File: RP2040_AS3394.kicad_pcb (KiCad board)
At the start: 4 copper layers, 123 parts, among them J1 Conn_01x03, J2 TYPE-C-31-M-12, U1 RP2040, U2 NCP1117-3.3_SOT223, U3 W25Q128JVS, U4 LM324, U5 AS3394, U6 LM324, Y1 X322512MSB4SI

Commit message: Started placement
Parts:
- R3, R4: footprint Resistor_SMD:R_0603_1608Metric -> Resistor_SMD:R_0402_1005Metric
- moved U6 160.7 mm to (181.6, 142.4)
- moved C25 148.5 mm to (172.8, 141.9)
- moved R26 137.7 mm to (169.8, 139.8)
- moved C22 136.3 mm to (165.1, 139.7)
- moved R23 135.9 mm to (165.5, 142.5)
- moved R13 133.7 mm to (158.1, 140.0)
- moved C48 131.6 mm to (178.4, 131.3)
- moved R18 131.1 mm to (161.3, 143.1)
- moved C47 130.0 mm to (178.2, 127.1)
- moved U5 129.0 mm to (131.1, 123.8)
- moved R10 127.3 mm to (155.1, 140.0)
- moved C20 126.0 mm to (162.4, 140.0)
- moved C24 111.1 mm to (83.7, 156.5)
- moved C21 109.4 mm to (75.7, 154.6)
- moved U4 107.5 mm to (102.5, 135.4)
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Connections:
- C22 pad 2: Net-(C22-Pad2) -> Net-(R26-Pad1)
- R23 pad 2: Net-(C22-Pad2) -> Net-(R26-Pad1)
- R26 pad 1: Net-(C22-Pad2) -> Net-(R26-Pad1)
- U4 pad 12: Net-(C20-Pad1) -> GND
- U4 pad 13: Net-(R18-Pad2) -> Net-(R43-Pad2)
- U4 pad 14: Net-(C22-Pad2) -> /AS3394_PWM/Wave_Select_CV
- U6 pad 1: /AS3394_PWM/Wave_Select_CV -> Net-(R26-Pad1)
- U6 pad 2: Net-(R43-Pad2) -> Net-(R18-Pad2)
- U6 pad 3: GND -> Net-(C20-Pad1)

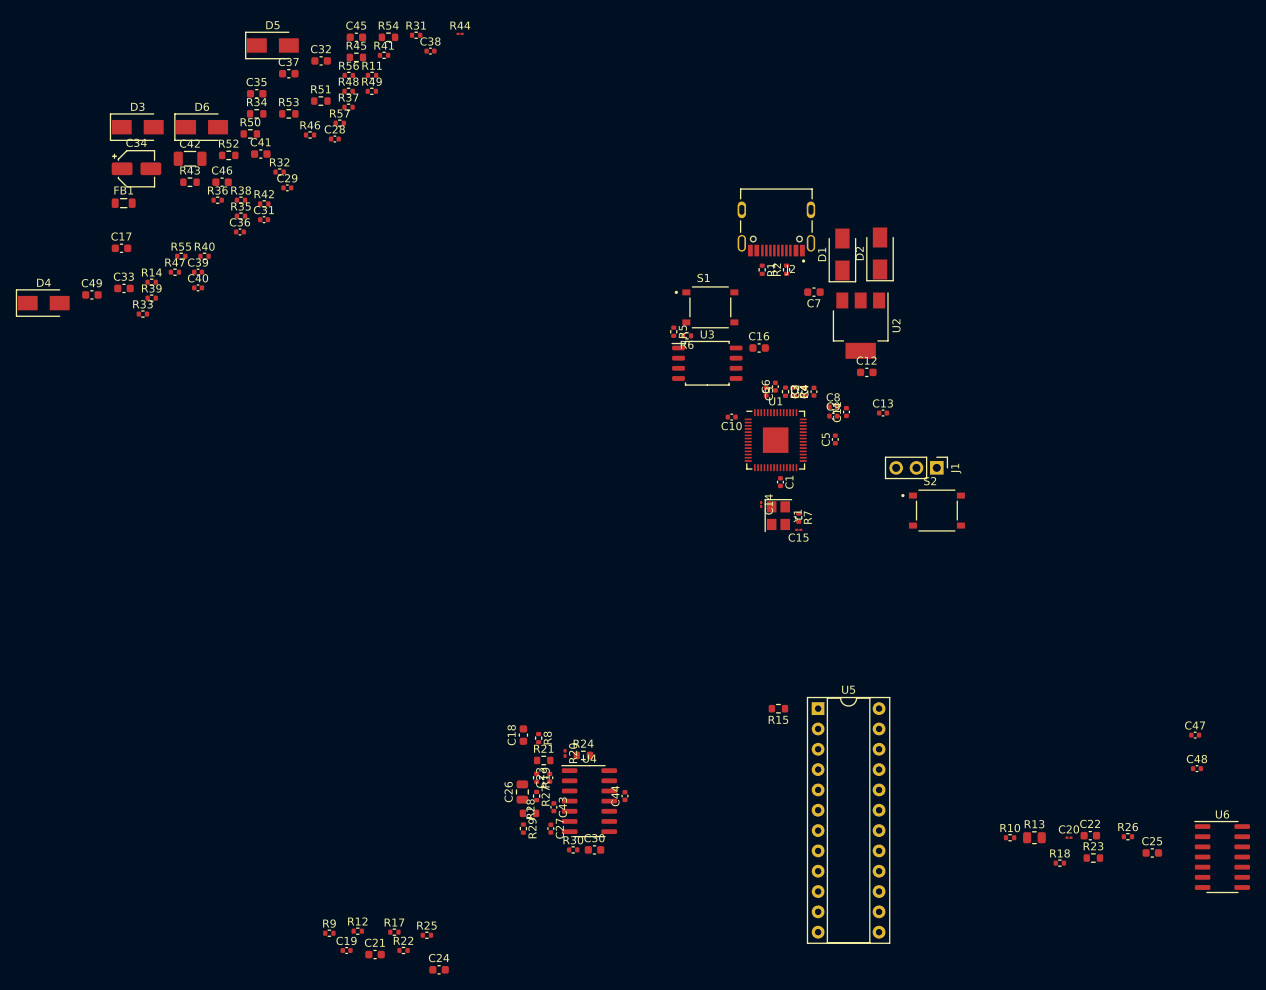
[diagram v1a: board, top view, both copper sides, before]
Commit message: Finished most of routing; added TL071 for headphone out; working on adding I/O
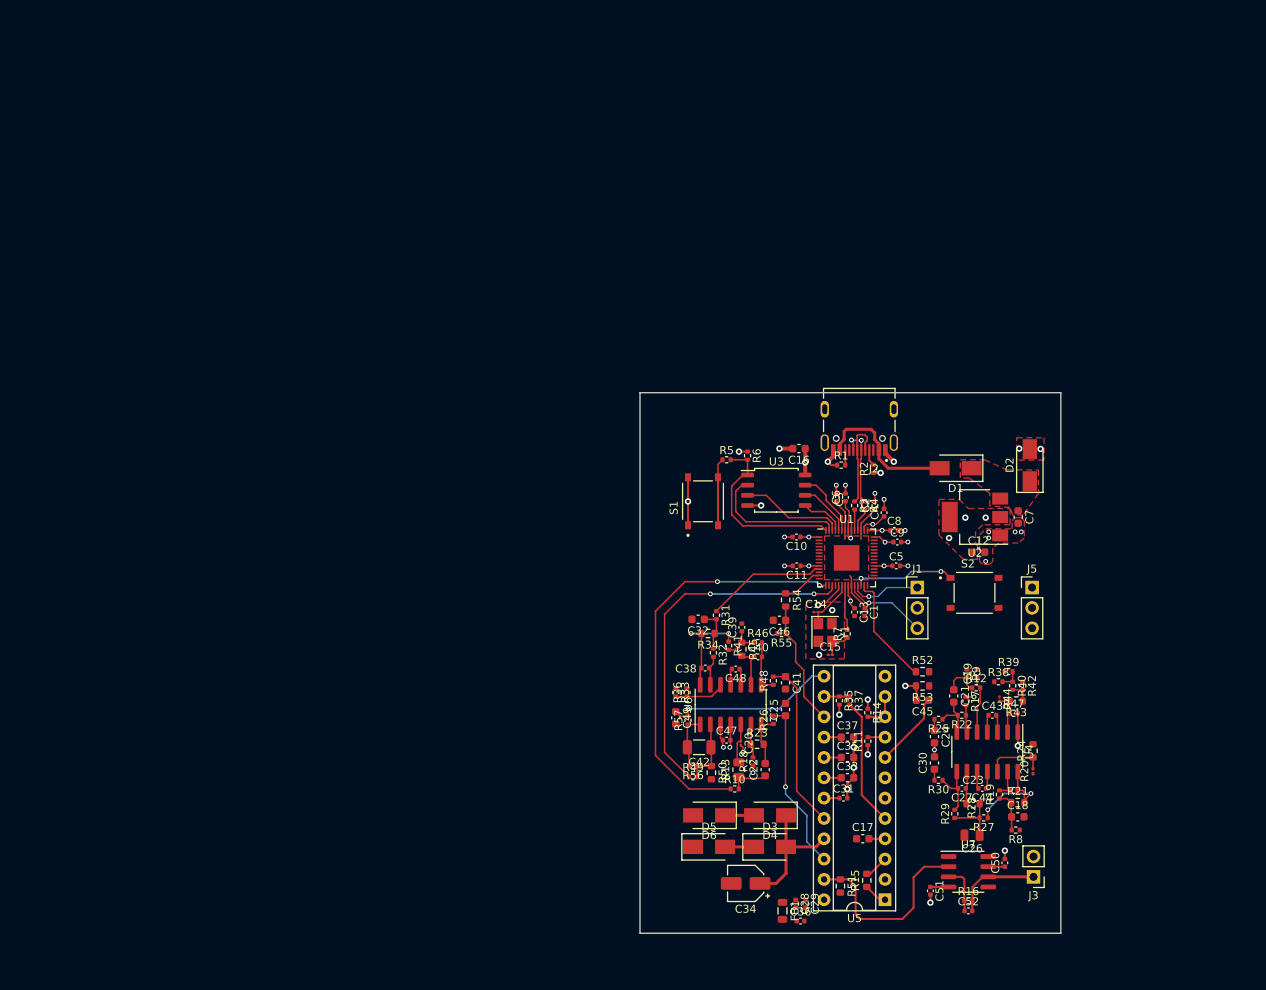
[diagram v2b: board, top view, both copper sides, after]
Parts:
- added C50: 0.1u, Capacitor_SMD:C_0402_1005Metric, F.Cu at (154.4, 143.1)
- added C51: 0.1u, Capacitor_SMD:C_0402_1005Metric, F.Cu at (145.1, 146.6)
- added C52: 47p, Capacitor_SMD:C_0402_1005Metric, F.Cu at (149.9, 149.1)
- added J3: Conn_01x02, Connector_PinHeader_2.54mm:PinHeader_1x02_P2.54mm_Vertical, F.Cu at (158.0, 144.8)
- added J5: Conn_01x03, Connector_PinHeader_2.54mm:PinHeader_1x03_P2.54mm_Vertical, F.Cu at (157.8, 108.7)
- added R16: 7.5k, Resistor_SMD:R_0402_1005Metric, F.Cu at (149.9, 147.8)
- added U7: TL071, Package_SO:SOIC-8_3.9x4.9mm_P1.27mm, F.Cu at (149.9, 144.2)
- moved R43 122.0 mm to (155.8, 122.9), turned to 180 degrees
- moved FB1 120.9 mm to (126.6, 149.1), turned to -90 degrees
- moved D3 119.8 mm to (125.1, 141.1)
- moved C17 118.5 mm to (136.7, 140.1)
- moved R47 118.5 mm to (155.5, 124.4)
- moved R51 117.7 mm to (133.9, 146.0), turned to -90 degrees
- moved C34 117.4 mm to (122.0, 145.7), turned to 180 degrees
- moved R39 116.8 mm to (154.9, 119.2)
- moved R40 114.4 mm to (155.4, 121.0), turned to -90 degrees
- moved D5 114.1 mm to (117.4, 141.1)
- moved R42 112.3 mm to (156.7, 121.0), turned to -90 degrees
- moved R38 112.2 mm to (153.6, 120.5)
- moved C28 111.6 mm to (128.3, 148.2), turned to -90 degrees
- moved D4 111.1 mm to (125.1, 137.2), turned to 180 degrees
- moved C35 111.1 mm to (134.7, 129.9)
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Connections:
- C22 pad 2: Net-(R26-Pad1) -> Net-(C22-Pad2)
- J2 pad S1: GND -> unconnected-(J2-PadS1)
- J2 pad S2: GND -> unconnected-(J2-PadS2)
- J2 pad S3: GND -> unconnected-(J2-PadS3)
- J2 pad S4: GND -> unconnected-(J2-PadS4)
- R23 pad 2: Net-(R26-Pad1) -> Net-(C22-Pad2)
- R26 pad 1: Net-(R26-Pad1) -> Net-(C22-Pad2)
- U1 pad 11: /AS3394_PWM/Final_Gain_PWM -> /AS3394_PWM/Filter_Freq_PWM
- U1 pad 13: /AS3394_PWM/Filter_Freq_PWM -> /AS3394_PWM/Filter_Res_PWM
- U1 pad 15: /AS3394_PWM/Filter_Res_PWM -> /AS3394_PWM/Final_Gain_PWM
- U1 pad 38: unconnected-(U1-Pad38) -> /AMP_OUT
- U4 pad 1: Net-(C23-Pad2) -> /AS3394_PWM/Wave_Select_CV
- U4 pad 10: Net-(C19-Pad1) -> GND
- U4 pad 12: GND -> Net-(R20-Pad2)
- U4 pad 13: Net-(R43-Pad2) -> Net-(C23-Pad1)
- U4 pad 14: /AS3394_PWM/Wave_Select_CV -> Net-(C23-Pad2)
- U4 pad 2: Net-(C23-Pad1) -> Net-(R43-Pad2)
- U4 pad 3: Net-(R20-Pad2) -> GND
- U4 pad 5: GND -> Net-(C19-Pad1)
- U4 pad 6: Net-(C27-Pad1) -> Net-(R17-Pad2)
- U4 pad 7: Net-(C27-Pad2) -> Net-(C21-Pad2)
- U4 pad 8: Net-(C21-Pad2) -> Net-(C27-Pad2)
- U4 pad 9: Net-(R17-Pad2) -> Net-(C27-Pad1)
- U6 pad 1: Net-(R26-Pad1) -> Net-(C42-Pad2)
- U6 pad 10: Net-(R33-Pad2) -> GND
- U6 pad 12: GND -> Net-(R33-Pad2)
- U6 pad 13: Net-(C40-Pad1) -> Net-(C38-Pad1)
- U6 pad 14: Net-(C40-Pad2) -> Net-(C38-Pad2)
- U6 pad 2: Net-(R18-Pad2) -> Net-(C42-Pad1)
- U6 pad 3: Net-(C20-Pad1) -> GND
- U6 pad 5: GND -> Net-(C20-Pad1)
- U6 pad 6: Net-(C42-Pad1) -> Net-(R18-Pad2)
- U6 pad 7: Net-(C42-Pad2) -> Net-(C22-Pad2)
- U6 pad 8: Net-(C38-Pad2) -> Net-(C40-Pad2)
- U6 pad 9: Net-(C38-Pad1) -> Net-(C40-Pad1)
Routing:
- net GND: track 0.00 -> 58.8 mm, vias 0 -> 37
- net /AS3394_PWM/Final_Gain_PWM: track 0.00 -> 52.3 mm, vias 0 -> 2
- net /AS3394_PWM/Mixer_Balance_PWM: track 0.00 -> 44.3 mm, vias 0 -> 2
- net +3V3: track 0.00 -> 30.8 mm, vias 0 -> 13
- net /AS3394_PWM/Out: track 0.00 -> 24.6 mm
- net /QSPI_SS: track 0.00 -> 22.7 mm
- net /AS3394_PWM/Final_Gain_CV: track 0.00 -> 21.4 mm, vias 0 -> 1
- net /AS3394_PWM/Mixer_Balance_CV: track 0.00 -> 21.4 mm, vias 0 -> 1
- net /AS3394_PWM/Filter_Freq_CV: track 0.00 -> 21.2 mm
- net Net-(D1-Pad2): track 0.00 -> 18.2 mm
- net /QSPI_SD1: track 0.00 -> 17.4 mm
- net Net-(C34-Pad1): track 0.00 -> 16.2 mm
- net /AS3394_PWM/Ext_Input2: track 0.00 -> 16.1 mm
- net /AS3394_PWM/Filter_Res_CV: track 0.00 -> 15.8 mm
- net /AS3394_PWM/Filter_Freq_PWM: track 0.00 -> 15.0 mm
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- added copper zone on F.Cu, net +1V1
- added copper zone on F.Cu, net +3V3
- added copper zone on In2.Cu, net +3V3
- added copper zone on F.Cu, net GND
- added copper zone on In1.Cu, net GND
- added copper zone on F.Cu, net Net-(C7-Pad1)
- added copper zone on F.Cu, net VCC
- added copper zone on In2.Cu, net VCC
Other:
- board outline added: 52.6 x 67.6 mm

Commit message: Mostly finished, just need to review and add final touches
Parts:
- added J4: Conn_01x08, Connector_PinHeader_2.54mm:PinHeader_1x08_P2.54mm_Vertical, F.Cu at (113.2, 88.0)
- moved S1 11.2 mm to (122.2, 88.1), turned to 0 degrees
- moved C36 3.41 mm to (126.2, 148.2), turned to -90 degrees
- moved FB1 2.99 mm to (127.3, 146.2), turned to 180 degrees
- moved C34 2.00 mm to (120.0, 145.7)
- moved C51 0.51 mm to (145.4, 146.2), turned to 90 degrees
- moved C10 0.38 mm to (128.4, 102.0)
- moved C11 0.24 mm to (128.3, 106.2)
- moved R5 0.05 mm to (119.7, 92.7)
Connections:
- U1 pad 2: unconnected-(U1-Pad2) -> Net-(U1-Pad2)
- U1 pad 28: /AS3394_PWM/Wave_Select_1 -> /AS3394_PWM/Wave_Select_2
- U1 pad 29: /AS3394_PWM/Wave_Select_2 -> /AS3394_PWM/Wave_Select_1
- U1 pad 3: unconnected-(U1-Pad3) -> Net-(U1-Pad3)
- U1 pad 4: unconnected-(U1-Pad4) -> Net-(U1-Pad4)
- U1 pad 5: unconnected-(U1-Pad5) -> Net-(U1-Pad5)
- U1 pad 6: unconnected-(U1-Pad6) -> Net-(U1-Pad6)
- U1 pad 7: unconnected-(U1-Pad7) -> Net-(U1-Pad7)
- U1 pad 8: unconnected-(U1-Pad8) -> Net-(U1-Pad8)
- U1 pad 9: unconnected-(U1-Pad9) -> Net-(U1-Pad9)
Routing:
- net /AMP_OUT: track 11.2 -> 67.7 mm, vias 0 -> 1
- net /AS3394_PWM/VCO_Freq_PWM: track 0.00 -> 51.8 mm
- net VEE: track 9.51 -> 52.3 mm, vias 0 -> 5
- net GND: track 58.8 -> 93.9 mm, vias 37 -> 65
- net Net-(U1-Pad2): track 0.00 -> 28.9 mm
- net Net-(U1-Pad3): track 0.00 -> 26.8 mm
- net /AS3394_PWM/Wave_Select_1: track 0.00 -> 26.6 mm, vias 0 -> 2
- net Net-(U1-Pad4): track 0.00 -> 24.6 mm
- net /AS3394_PWM/Wave_Select_2: track 0.00 -> 23.9 mm, vias 0 -> 2
- net Net-(U1-Pad5): track 0.00 -> 21.6 mm
- net /AS3394_PWM/Mod_Amt_PWM: track 0.00 -> 20.7 mm
- net Net-(U1-Pad6): track 0.00 -> 20.6 mm
- net Net-(U1-Pad7): track 0.00 -> 19.7 mm
- net Net-(U1-Pad8): track 0.00 -> 18.8 mm
- net /AS3394_PWM/Wave_Select_CV: track 4.07 -> 22.3 mm
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- added copper zone on F.Cu, net Net-(C28-Pad1)
- added copper zone on F.Cu, net VEE
- added copper zone on In2.Cu, net VEE

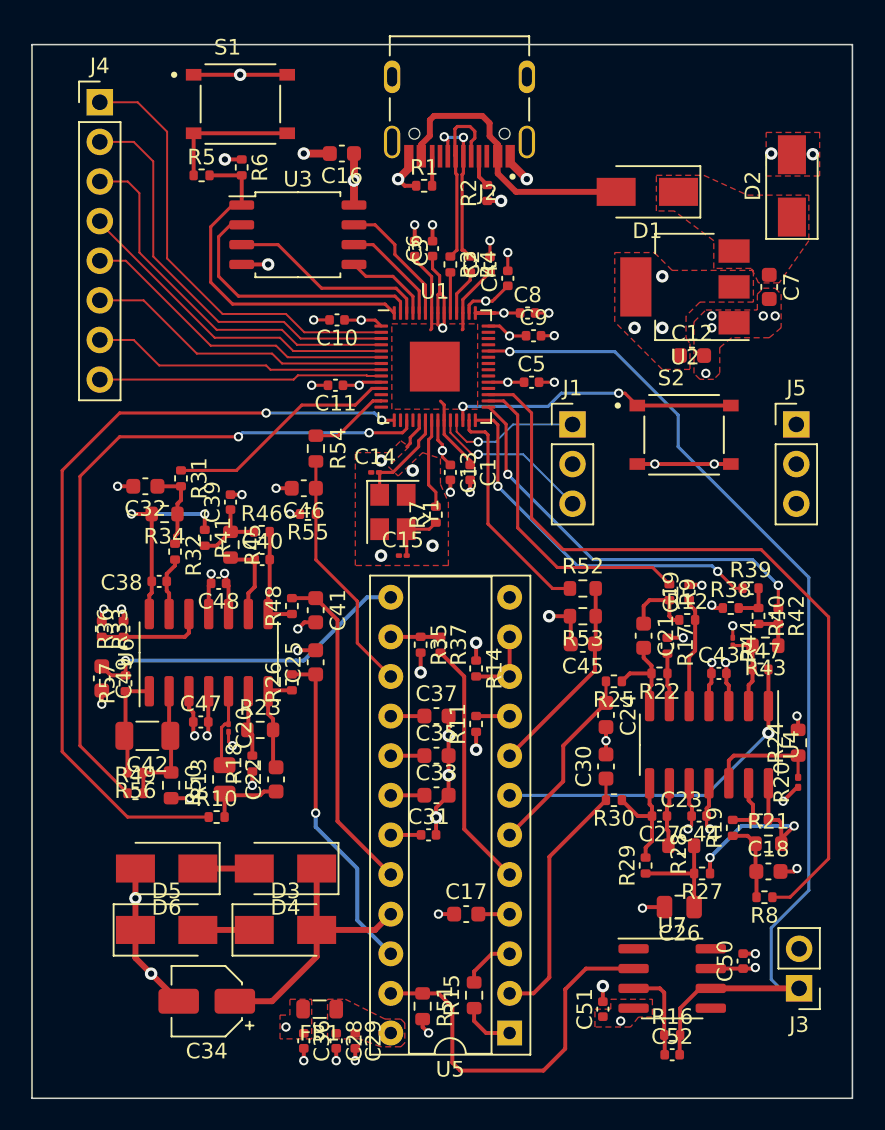
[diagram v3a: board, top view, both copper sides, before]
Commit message: Moved silkscreen designators so they're mostly readable. Rerouted some traces on bottom layer so they don't cross power planes with different potentials
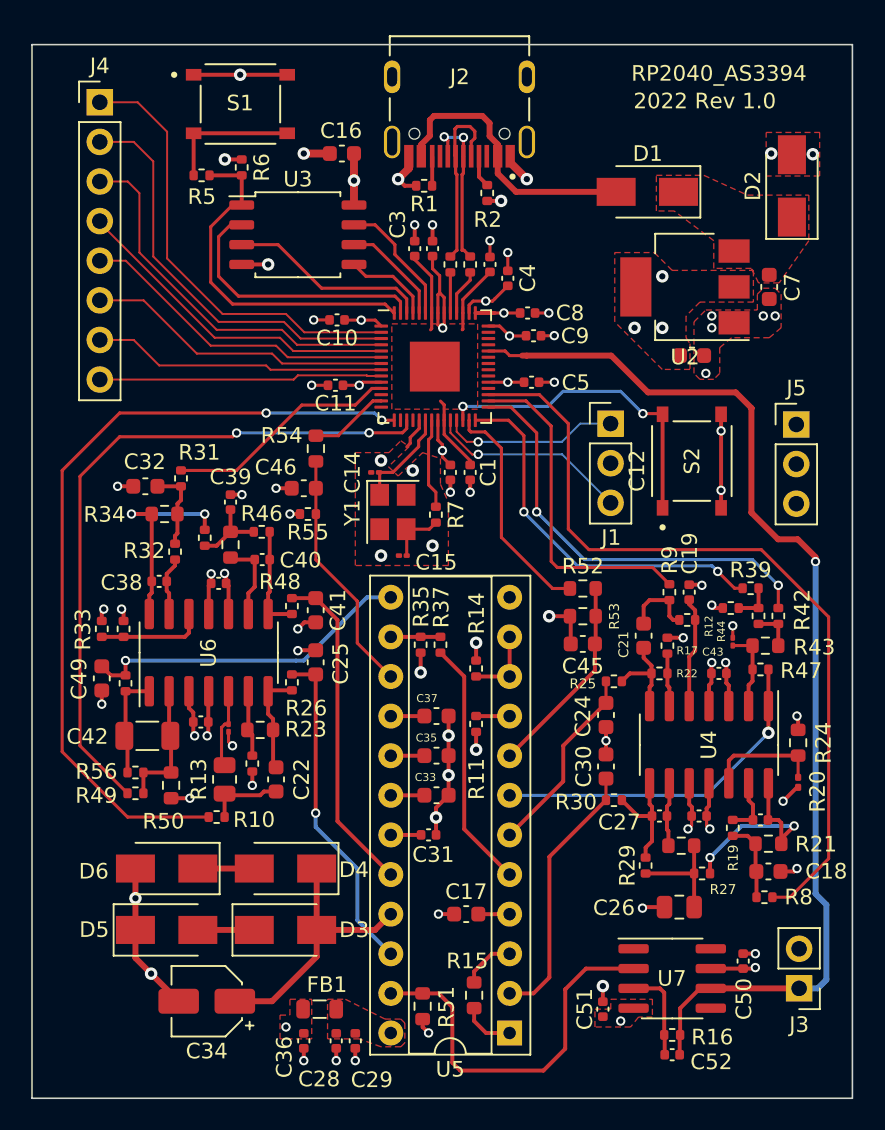
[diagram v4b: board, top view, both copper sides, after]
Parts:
- moved J1 2.44 mm to (145.9, 108.6)
- moved S2 1.76 mm to (151.1, 111.0), turned to 90 degrees
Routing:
- net /AMP_OUT: track 67.7 -> 71.2 mm
- net Net-(J1-Pad1): track 8.90 -> 11.4 mm
- net Net-(J1-Pad3): track 10.5 -> 12.9 mm
- net /RUN: track 18.9 -> 20.9 mm
- net /AS3394_PWM/Wave_Select_1: track 26.6 -> 27.7 mm
- net /AS3394_PWM/Mod_Amt_PWM: track 20.7 -> 21.6 mm
- net /AS3394_PWM/Wave_Select_2: track 23.9 -> 24.5 mm
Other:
- board text added: "2022 Rev 1.0"
- board text added: "RP2040_AS3394"
